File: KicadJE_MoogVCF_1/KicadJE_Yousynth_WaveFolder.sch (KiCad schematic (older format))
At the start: 64 parts

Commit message: Wavefolder annotated
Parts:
- removed C?: 10n, Capacitor_SMD:C_0805_2012Metric_Pad1.15x1.40mm_HandSolder, symbol Device:C
- removed C?: Opt_220u, Capacitor_THT:CP_Radial_D10.0mm_P5.00mm, symbol Device:CP
- added C406, C407: 10n opt, Capacitor_SMD:C_0805_2012Metric_Pad1.15x1.40mm_HandSolder, symbol Device:C
- added D408, D409, D410, D411, D412, D413, D414, D415, D416, D417, D418, D419, D420, D421, D422, D423, D424, D425, D426, D427: LL4148, Diode_SMD:D_MiniMELF, symbol Diode:LL4148
- added R406, R411, R433: 5k6, Resistor_SMD:R_0805_2012Metric_Pad1.15x1.40mm_HandSolder, symbol Device:R
- added R416, R419, R424, R427, R429, R431, R434, R438: 15k, Resistor_SMD:R_0805_2012Metric_Pad1.15x1.40mm_HandSolder, symbol Device:R
- added R426, R430: 56k, Resistor_SMD:R_0805_2012Metric_Pad1.15x1.40mm_HandSolder, symbol Device:R
- added R428: 27k, Resistor_SMD:R_0805_2012Metric_Pad1.15x1.40mm_HandSolder, symbol Device:R
- added R432: 0R, Resistor_SMD:R_0805_2012Metric_Pad1.15x1.40mm_HandSolder, symbol Device:R
- added RV405: 100k CV, Potentiometer_THT:Potentiometer_China_RK09_Single_Vertical_AJ, symbol Device:R_POT
- C408: renamed from C?; value 22u -> 22u Opt
- R435: renamed from R?; value 220R -> Open
- gave numbers to parts that had none: 53
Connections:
- wire segments 176 -> 326
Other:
- moved on the sheet: C408, R435, R436, R437, R439, R440, SW401, U402A, U402B, U402C, U402D

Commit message: ERC done
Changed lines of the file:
@@
 Wire Wire Line
 	5425 6125 5375 6125
+$Comp
+L power:PWR_FLAG #FLG0101
+U 1 1 600415DD
+P 4050 775
+F 0 "#FLG0101" H 4050 850 50  0001 C CNN
+F 1 "PWR_FLAG" H 4050 948 50  0000 C CNN
+F 2 "" H 4050 775 50  0001 C CNN
+F 3 "~" H 4050 775 50  0001 C CNN
+	1    4050 775
+	1    0    0    -1
+$EndComp
+Connection ~ 4050 775
+$Comp
+L power:PWR_FLAG #FLG0102
+U 1 1 60042A0E
+P 4050 1475
+F 0 "#FLG0102" H 4050 1550 50  0001 C CNN
+F 1 "PWR_FLAG" H 4050 1648 50  0000 C CNN
+F 2 "" H 4050 1475 50  0001 C CNN
+F 3 "~" H 4050 1475 50  0001 C CNN
+	1    4050 1475
+	-1   0    0    1
+$EndComp
+$Comp
+L power:PWR_FLAG #FLG0103
+U 1 1 6004550D
+P 3675 1125
+F 0 "#FLG0103" H 3675 1200 50  0001 C CNN
+F 1 "PWR_FLAG" H 3675 1298 50  0000 C CNN
+F 2 "" H 3675 1125 50  0001 C CNN
+F 3 "~" H 3675 1125 50  0001 C CNN
+	1    3675 1125
+	1    0    0    -1
+$EndComp
+Connection ~ 3675 1125
 $EndSCHEMATC

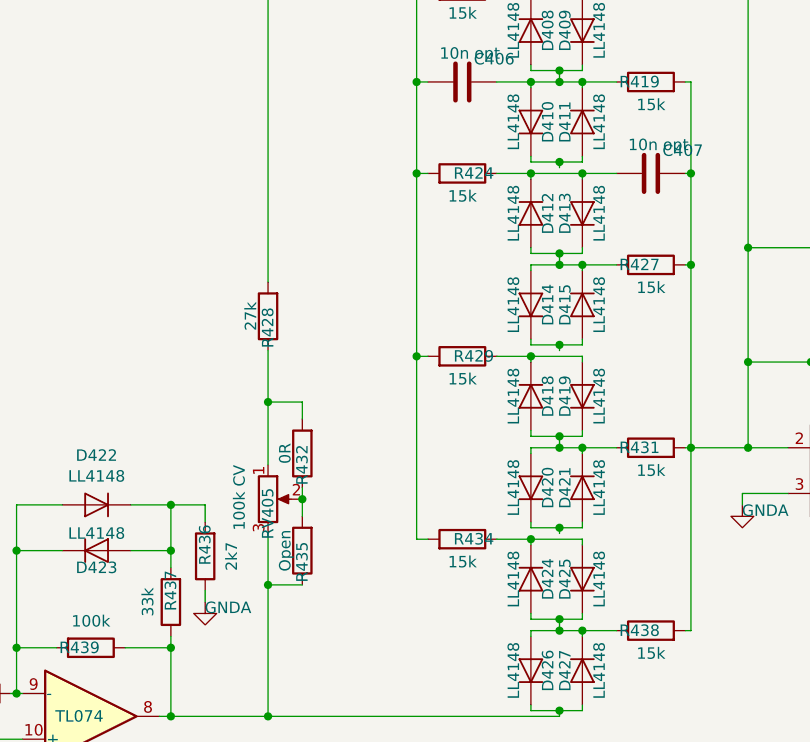
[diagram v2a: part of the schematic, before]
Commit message: Folding Diode conn missing
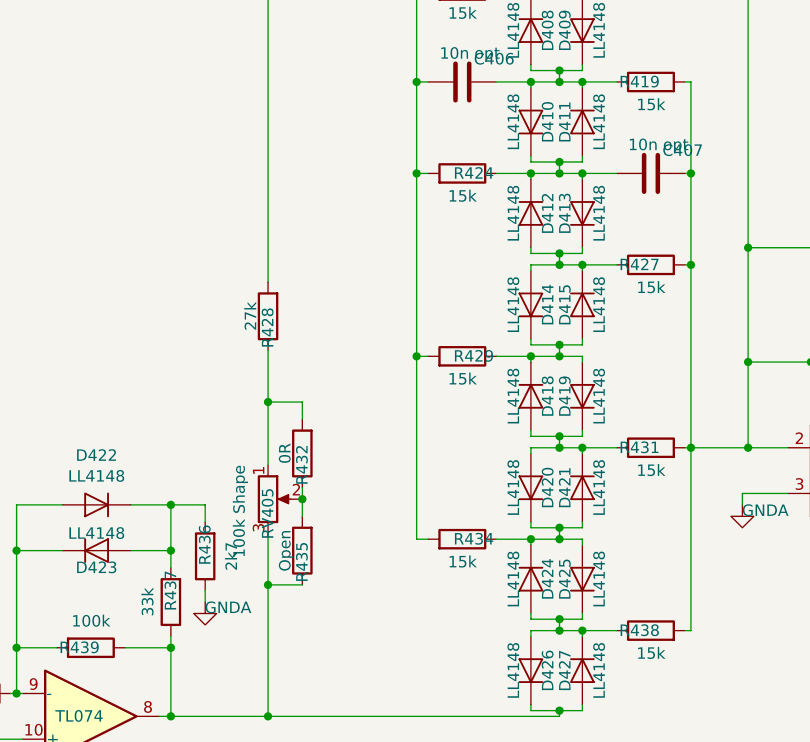
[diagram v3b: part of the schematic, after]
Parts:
- RV405: value 100k CV -> 100k Shape
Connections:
- net at D424.1 (K), D425.2 (A), R434.1: now also D420.1 (K), D421.2 (A)
- net at D418.1 (K), D419.2 (A), R429.1: now also D414.1 (K), D415.2 (A)
- net at C407.2, D412.1 (K), D413.2 (A)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: now also D410.1 (K), D411.2 (A)
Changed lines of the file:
@@
 AR Path="/5F56E895/5F8B6317" Ref="RV405"  Part="1"
 F 0 "RV405" V 2400 6300 50  0000 R CNN
-F 1 "100k CV" V 2275 6400 50  0000 R CNN
+F 1 "100k Shape" V 2275 6400 50  0000 R CNN
 F 2 "Potentiometer_THT:Potentiometer_China_RK09_Single_Vertical_AJ" H 2400 6250 50  0001 C CNN
 F 3 "~" H 2400 6250 50  0001 C CNN
@@
 	3775 6450 3775 6425
 Wire Wire Line
-	3775 6425 3550 6425
+	3775 6425 3675 6425
 Wire Wire Line
 	3550 6425 3550 6450
@@
 Wire Wire Line
 	3775 6025 3775 6050
-Wire Wire Line
-	3675 6400 3675 6375
 Connection ~ 3675 6375
 Wire Wire Line
@@
 	3775 5650 3775 5625
 Wire Wire Line
-	3775 5625 3550 5625
+	3775 5625 3675 5625
 Wire Wire Line
 	3550 5625 3550 5650
@@
 Wire Wire Line
 	3775 5225 3775 5250
-Wire Wire Line
-	3675 5600 3675 5575
 Connection ~ 3675 5575
 Wire Wire Line
@@
 	3775 4850 3775 4825
 Wire Wire Line
-	3775 4825 3550 4825
+	3775 4825 3675 4825
 Wire Wire Line
 	3550 4825 3550 4850
@@
 Wire Wire Line
 	3775 4425 3775 4450
-Wire Wire Line
-	3675 4800 3675 4775
 Connection ~ 3675 4775
 Wire Wire Line
@@
 $EndComp
 Connection ~ 3675 1125
+Wire Wire Line
+	3675 6375 3675 6425
+Connection ~ 3675 6425
+Wire Wire Line
+	3675 6425 3550 6425
+Wire Wire Line
+	3675 5575 3675 5625
+Connection ~ 3675 5625
+Wire Wire Line
+	3675 5625 3550 5625
+Wire Wire Line
+	3675 4775 3675 4825
+Connection ~ 3675 4825
+Wire Wire Line
+	3675 4825 3550 4825
 $EndSCHEMATC

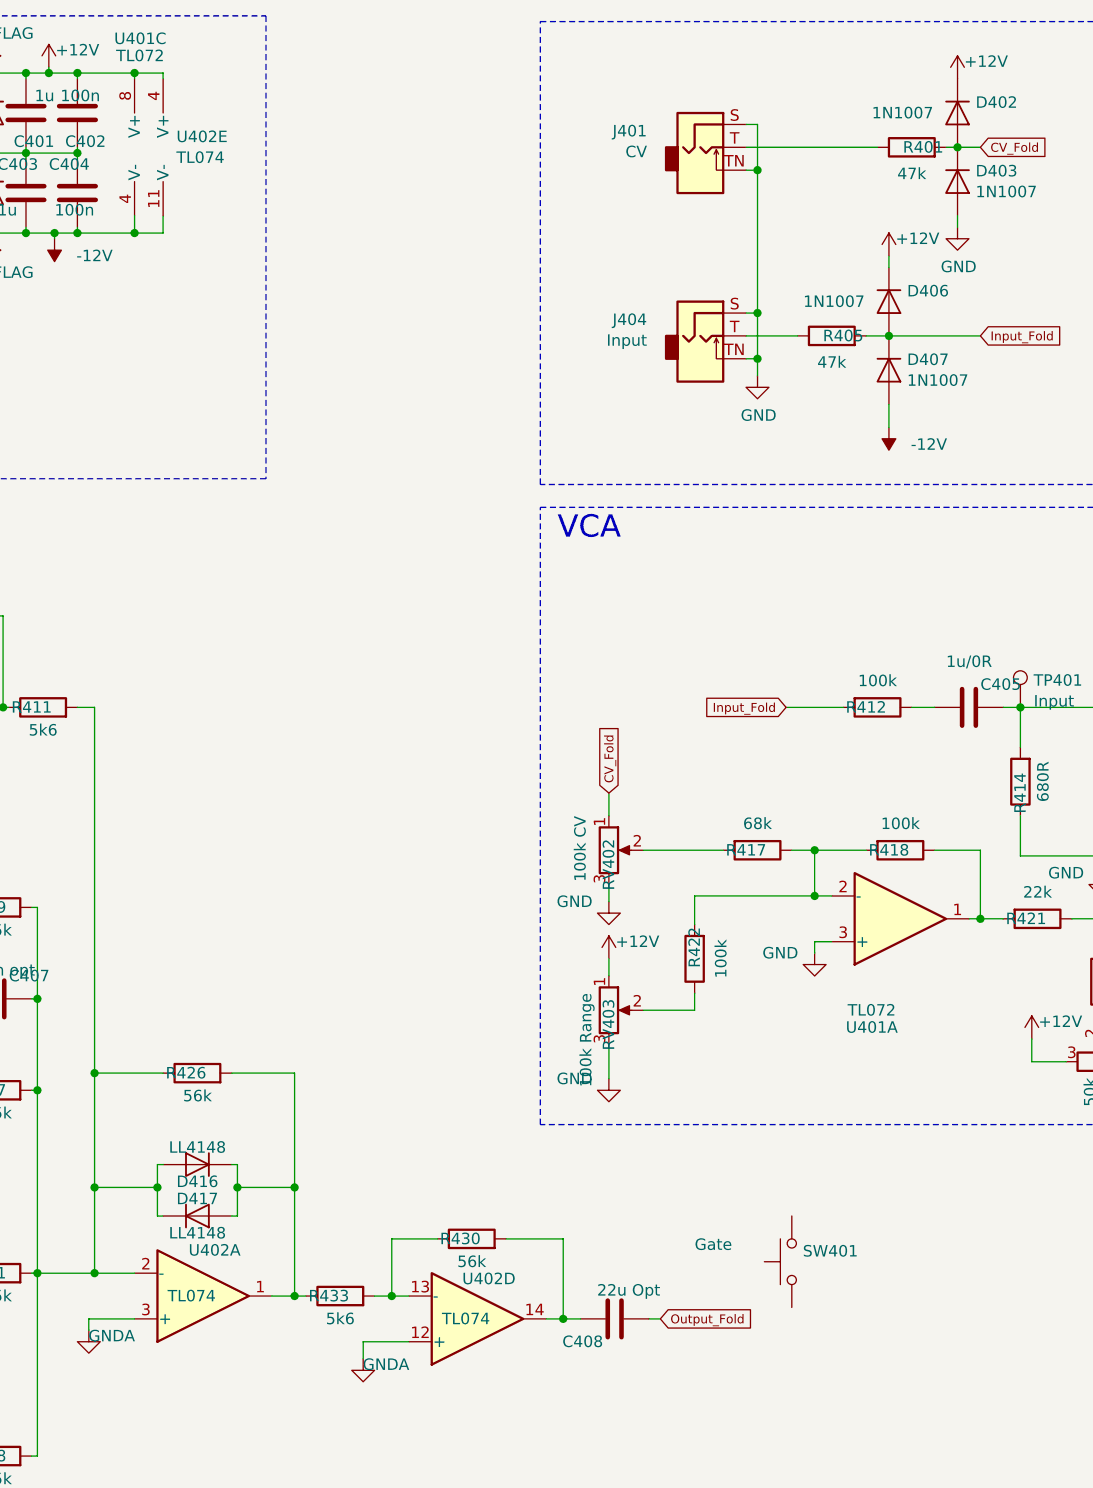
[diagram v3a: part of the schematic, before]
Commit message: Wavefolder labeled
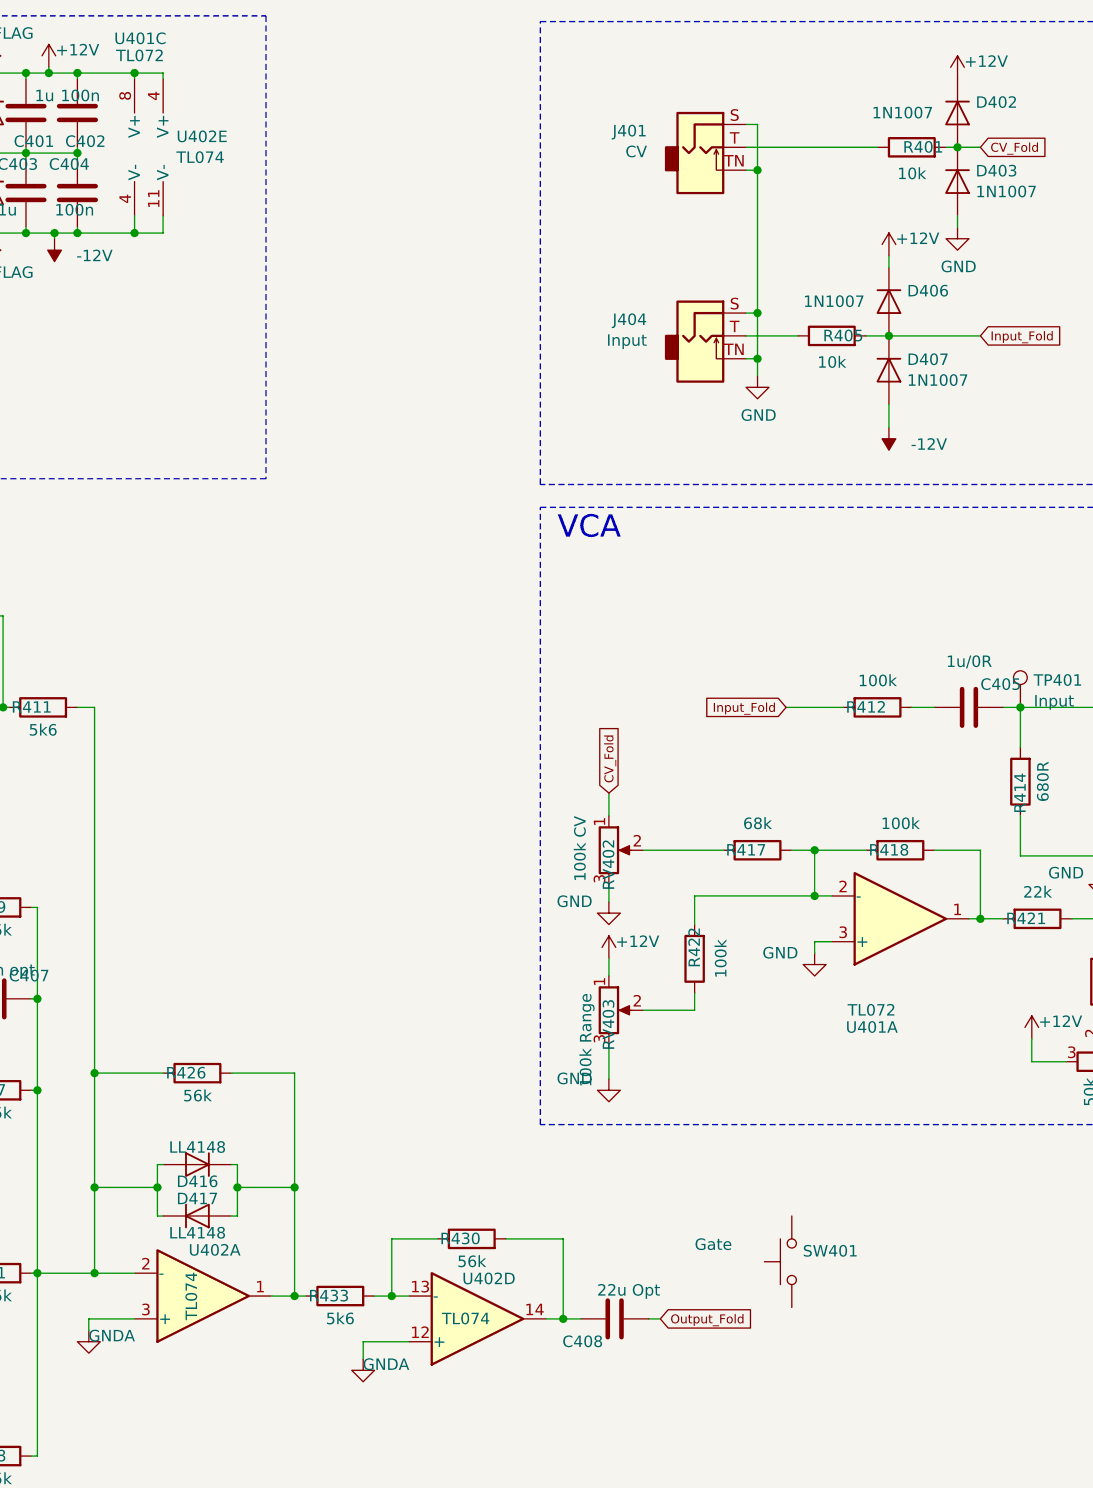
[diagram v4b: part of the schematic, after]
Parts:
- R401, R405: value 47k -> 10k
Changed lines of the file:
@@
 AR Path="/5F56E895/5F57E6FF" Ref="R401"  Part="1"
 F 0 "R401" V 8075 1050 50  0000 C CNN
-F 1 "47k" V 7959 1100 50  0000 C CNN
+F 1 "10k" V 7959 1100 50  0000 C CNN
 F 2 "Resistor_SMD:R_0805_2012Metric_Pad1.15x1.40mm_HandSolder" V 8005 1100 50  0001 C CNN
 F 3 "~" H 8075 1100 50  0001 C CNN
@@
 AR Path="/5F56E895/5F5888D7" Ref="R405"  Part="1"
 F 0 "R405" V 7725 1875 50  0000 C CNN
-F 1 "47k" V 7609 1925 50  0000 C CNN
+F 1 "10k" V 7609 1925 50  0000 C CNN
 F 2 "Resistor_SMD:R_0805_2012Metric_Pad1.15x1.40mm_HandSolder" V 7655 1925 50  0001 C CNN
 F 3 "~" H 7725 1925 50  0001 C CNN
@@
 P 4975 6125
 F 0 "U402" H 5025 5925 50  0000 C CNN
-F 1 "TL074" H 4925 6125 50  0000 C CNN
+F 1 "TL074" V 4925 6125 50  0000 C CNN
 F 2 "" H 4925 6225 50  0001 C CNN
 F 3 "http://www.ti.com/lit/ds/symlink/tl071.pdf" H 5025 6325 50  0001 C CNN

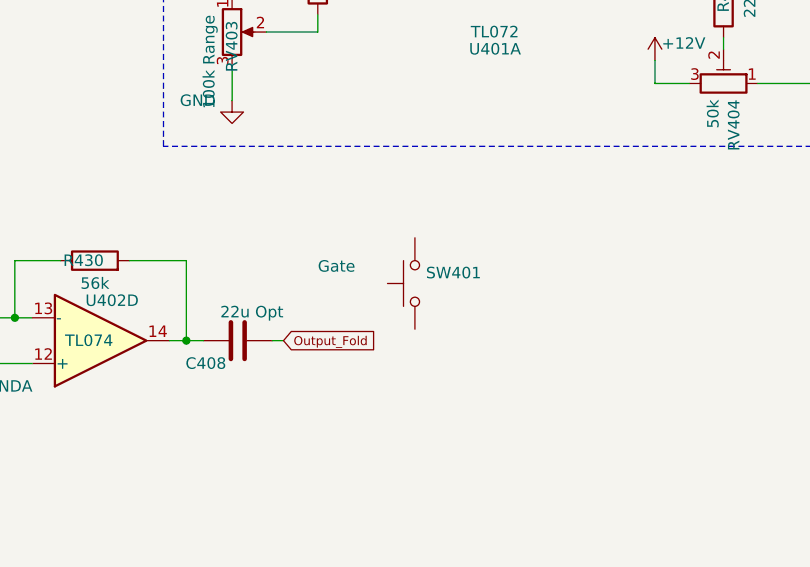
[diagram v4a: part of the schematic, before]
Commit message: remove excess btn
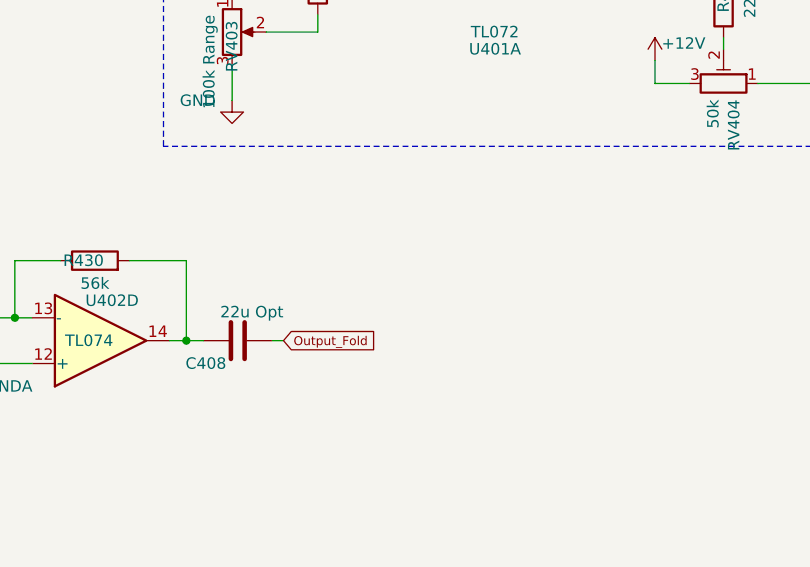
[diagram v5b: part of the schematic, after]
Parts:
- removed SW401: Gate, Button_Switch_THT:SW_PUSH_6mm, symbol Envelope-cache-2018-08-04-13-00-04:SW_Push
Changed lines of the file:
@@
-$EndComp
-$Comp
-L Envelope-cache-2018-08-04-13-00-04:SW_Push SW?
-U 1 1 5F578E81
-P 7550 5975
-AR Path="/5F18E4B5/5F578E81" Ref="SW?"  Part="1"
-AR Path="/5F56E895/5F578E81" Ref="SW401"  Part="1"
-F 0 "SW401" V 7596 5927 50  0000 R CNN
-F 1 "Gate" V 7625 6400 50  0000 R CNN
-F 2 "Button_Switch_THT:SW_PUSH_6mm" H 7550 6175 50  0001 C CNN
-F 3 "" H 7550 6175 50  0001 C CNN
-	1    7550 5975
-	0    -1   -1   0
 $EndComp
 $Comp
